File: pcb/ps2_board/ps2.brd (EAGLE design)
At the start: 56 x 65 mm, 12 parts, among them IC3 STM32F042F4, J1 DIN7, J2 DIN7, SW4 324_SW

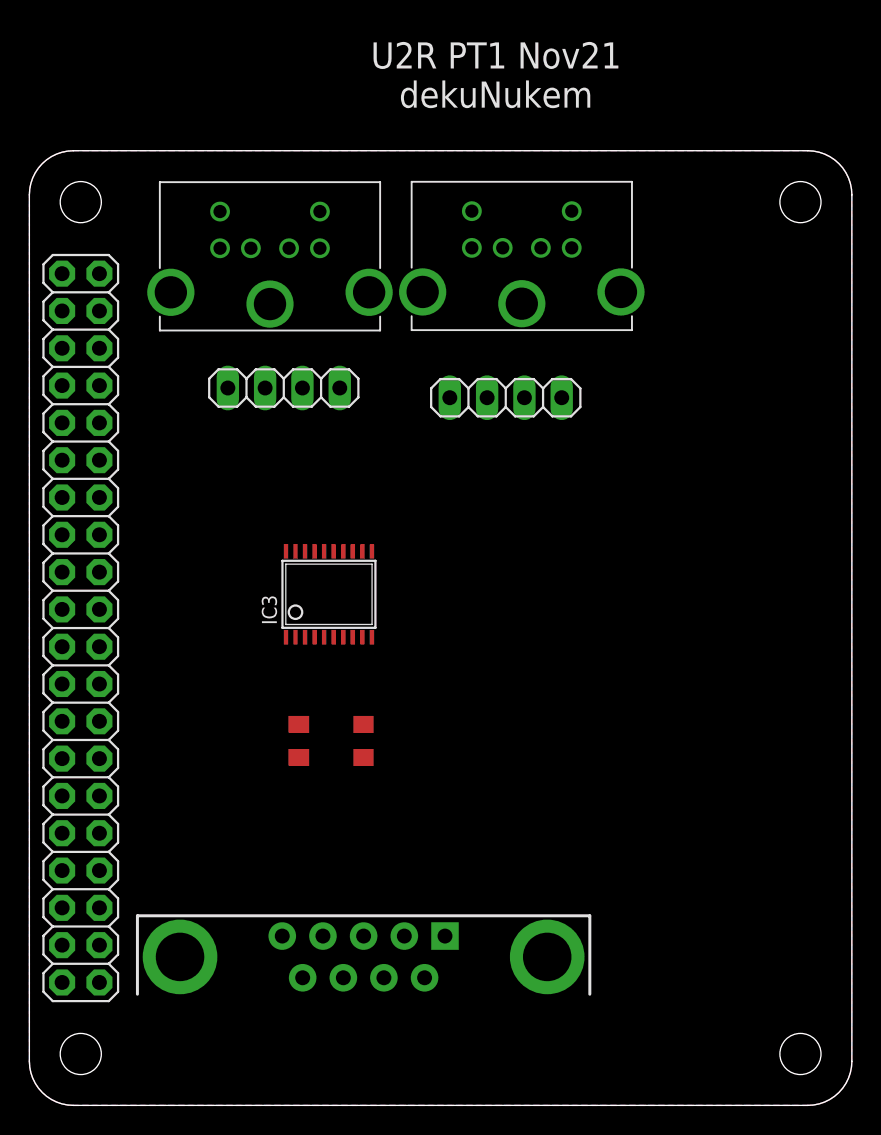
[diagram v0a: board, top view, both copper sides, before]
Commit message: ps2 board done apart from max232
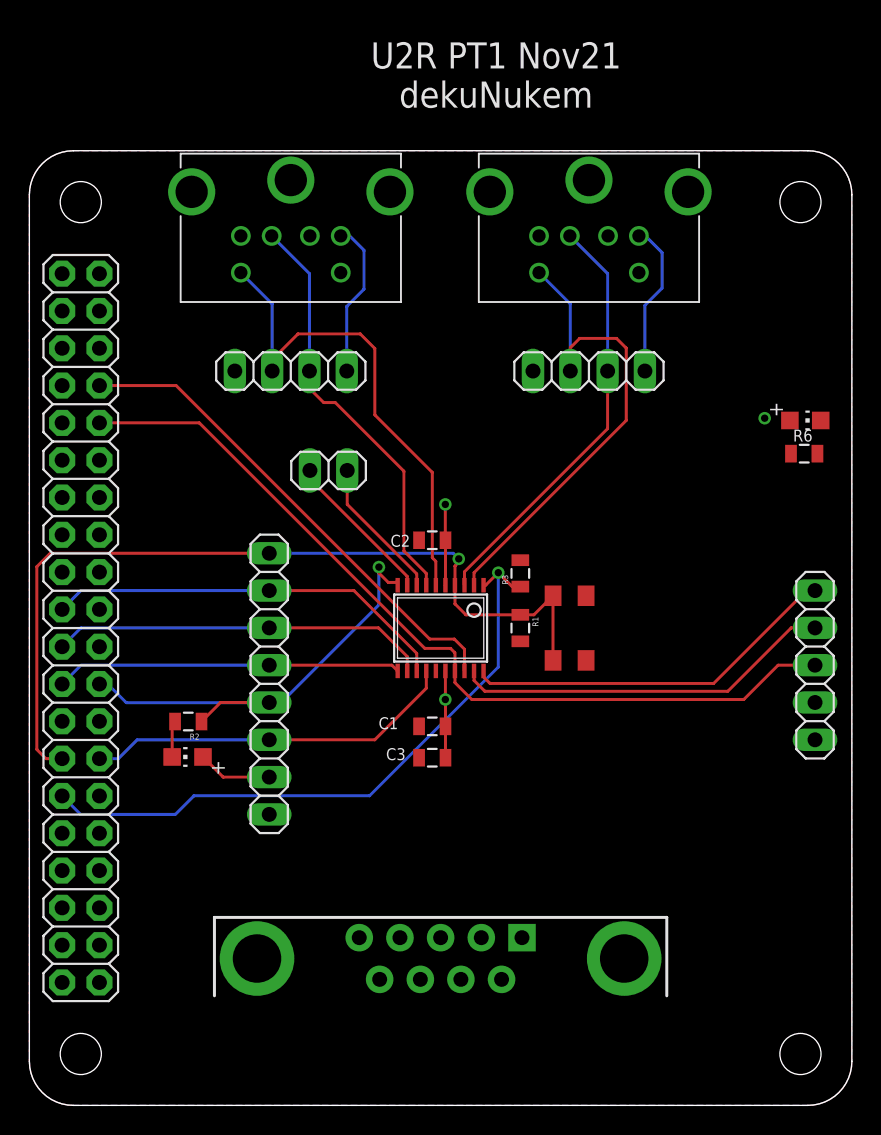
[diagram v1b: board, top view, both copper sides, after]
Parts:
- added C1, C2, C3: 100nF, clock:0805@1
- added JP4: (no value), pinhead:1X08
- added JP5: (no value), pinhead:1X05
- added JP6: (no value), pinhead:1X02
- added LED1, LED2: (no value), adafruit:CHIP-LED0805
- added R1, R3: 10K, SparkFun-Passives:0805
- added R2, R6: 1K, SparkFun-Passives:0805
- J1, J2: value DIN7 -> (none)
- moved JP2 20.8 mm to (38.1, 50.0)
- moved SW4 18.0 mm to (36.8, 32.5), turned to 90 degrees
- moved JP3 14.7 mm to (17.8, 50.0)
- moved J1 9.58 mm to (38.1, 63.0), turned to 0 degrees
- moved J2 8.56 mm to (17.8, 63.0), turned to 0 degrees
- moved IC3 7.94 mm to (28.0, 32.5), turned to 180 degrees
- moved J3 5.24 mm to (28.0, 10.0)
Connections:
- new net N$1: IC3.4, JP1.27, JP4.8, R1.1, SW4.P$2, SW4.P$3
- new net N$10: IC3.8, JP6.1
- new net N$11: IC3.9, JP6.2
- new net N$2: LED1.C, R2.2
- new net N$29: LED2.C, R6.2
- new net N$3: J1.4_5V, JP2.4
- new net N$4: J2.4_5V, JP3.4
- new net N$5: IC3.2, J1.5_CLK, JP2.2
- new net N$6: IC3.3, J1.1_DATA, JP2.3
- new net N$7: IC3.6, J2.5_CLK, JP3.2
- new net N$8: IC3.7, J2.1_DATA, JP3.3
- new net N$9: IC3.1, JP1.29, R3.1
- new net SLAVE_REQ: IC3.14, JP1.28, JP4.3
- new net SPI1_CS: IC3.10, JP1.24, JP4.4, R2.1
- new net SPI1_MISO: IC3.12, JP1.21, JP4.6
- new net SPI1_MOSI: IC3.13, JP1.19, JP4.7
- new net SPI1_SCK: IC3.11, JP1.23, JP4.5
- new net STM32_RX: IC3.18, JP1.8
- new net STM32_TX: IC3.17, JP1.10, JP5.3
- new net SWCLK: IC3.20, JP5.5
- new net SWDIO: IC3.19, JP5.4
- net +3V3: now also C1.2, C2.2, C3.2, IC3.16, IC3.5, JP4.2, JP5.2, LED1.A, LED2.A
- net GND: now also C1.1, C2.1, C3.1, IC3.15, J1.3_GND, J1.SHIELD1, J1.SHIELD2, J1.SHIELD3, J2.3_GND, J2.SHIELD1, J2.SHIELD2, J2.SHIELD3, JP2.1, JP3.1, JP4.1, JP5.1, R1.2, R3.2, R6.1, SW4.P$1, SW4.P$4
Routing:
- net N$1: track 0.00 -> 58.8 mm, vias 0 -> 1
- net STM32_TX: track 0.00 -> 58.7 mm
- net N$9: track 0.00 -> 44.0 mm, vias 0 -> 1
- net N$7: track 0.00 -> 34.3 mm
- net N$5: track 0.00 -> 34.0 mm
- net STM32_RX: track 0.00 -> 33.8 mm
- net SPI1_CS: track 0.00 -> 32.2 mm, vias 0 -> 1
- net N$6: track 0.00 -> 28.9 mm
- net N$8: track 0.00 -> 28.6 mm
- net SPI1_MOSI: track 0.00 -> 27.6 mm
- net SWDIO: track 0.00 -> 26.0 mm
- net SPI1_MISO: track 0.00 -> 25.8 mm
- net SWCLK: track 0.00 -> 25.8 mm
- net SLAVE_REQ: track 0.00 -> 25.4 mm
- net SPI1_SCK: track 0.00 -> 23.5 mm
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
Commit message: ps2 board prototype done
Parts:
- added C4, C5, C6, C7, C9: 100nF, clock:0805@1
- added JP10: (no value), pinhead:2X04
- added JP11, JP7, JP8, JP9: (no value), pinhead:1X04
- added U1: MAX3232, SparkFun-DigitalIC:SO016
- moved LED2 52.5 mm to (11.9, 13.7)
- moved R6 47.9 mm to (16.0, 13.7), turned to 180 degrees
- moved J3 6.30 mm to (28.8, 3.75)
- moved SW4 3.51 mm to (36.8, 36.0)
- moved J1 1.27 mm to (38.1, 61.7)
- moved J2 1.27 mm to (17.8, 61.7)
- moved JP2 1.27 mm to (38.1, 48.7)
- moved JP3 1.27 mm to (17.8, 48.7)
- moved C3 1.19 mm to (27.4, 24.9)
- moved C1 1.12 mm to (27.4, 26.9)
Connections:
- new net C1+: C9.1, U1.1
- new net C1-: C9.2, U1.3
- new net C2+: C4.1, U1.4
- new net C2-: C4.2, U1.5
- new net N$12: JP8.1, U1.10
- new net N$13: JP8.2, U1.9
- new net N$14: JP8.3, U1.7
- new net N$15: JP8.4, U1.8
- new net N$16: J3.1, JP10.2
- new net N$17: J3.2, JP10.4
- new net N$18: J3.3, JP10.6
- new net N$19: J3.4, JP10.8
- new net N$20: J3.6, JP10.1
- new net N$21: J3.7, JP10.3
- new net N$22: J3.8, JP10.5
- new net N$23: J3.9, JP10.7
- new net RX1IN_232: JP7.2, U1.13
- new net TX1OUT_232: JP7.1, U1.14
- new net V+: C6.1, U1.2
- new net V-: C5.1, U1.6
- net +3V3: now also C7.1, JP11.1, JP11.2, JP11.3, JP11.4, U1.16
- net GND: now also C5.2, C6.2, C7.2, J3.5, J3.G1, J3.G2, JP9.1, JP9.2, JP9.3, JP9.4, U1.15
- net STM32_RX: now also JP7.3, U1.12
- net STM32_TX: now also JP7.4, U1.11
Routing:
- net STM32_RX: track 33.8 -> 92.3 mm
- net +3V3: track 16.5 -> 40.9 mm, vias 3 -> 1
- net N$16: track 0.00 -> 8.93 mm
- net STM32_TX: track 58.7 -> 67.5 mm
- net N$19: track 0.00 -> 8.79 mm
- net N$18: track 0.00 -> 8.68 mm
- net N$17: track 0.00 -> 8.60 mm
- net N$23: track 0.00 -> 8.59 mm
- net N$22: track 0.00 -> 8.50 mm
- net N$21: track 0.00 -> 8.41 mm
- net N$20: track 0.00 -> 8.31 mm
- net N$14: track 0.00 -> 6.64 mm
- net N$12: track 0.00 -> 6.12 mm
- net TX1OUT_232: track 0.00 -> 5.55 mm
- net RX1IN_232: track 0.00 -> 5.03 mm
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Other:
- board text added: "3V3"
- board text added: "5V"
- board text added: "C"
- board text added: "CLK"
- board text added: "CS"
- board text added: "D"
- board text added: "DIO"
- board text added: "GND"
- board text added: "KEYBOARD"
- board text added: "MISO"
- board text added: "MOSI"
- board text added: "MOUSE"
- board text added: "PA2"
- board text added: "PA3"
- board text added: "POWER"
- board text added: "R1IN"
- board text added: "R1OUT"
- board text added: "R2IN"
- board text added: "R2OUT"
- board text added: "SCK"
- board text added: "STM32 RST"
- board text added: "S_REQ"
- board text added: "T1IN"
- board text added: "T1OUT"
- board text added: "T2IN"
- board text added: "T2OUT"
- board text added: "TX"
- board text added: "U2R PS2 PT1 Nov21 dekuNukem"
- board text removed: "U2R PT1 Nov21 dekuNukem"
